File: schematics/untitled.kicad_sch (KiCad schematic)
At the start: 9 parts, among them U1 LM358, U2 LM358

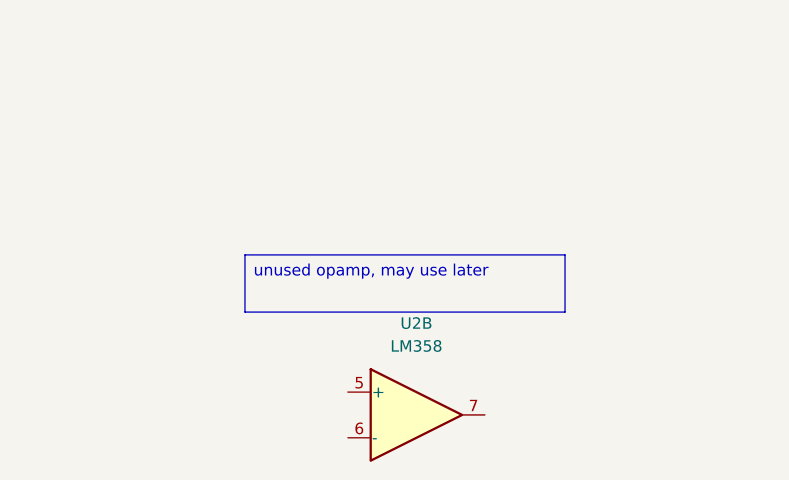
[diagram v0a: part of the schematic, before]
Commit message: added titles to all sheets
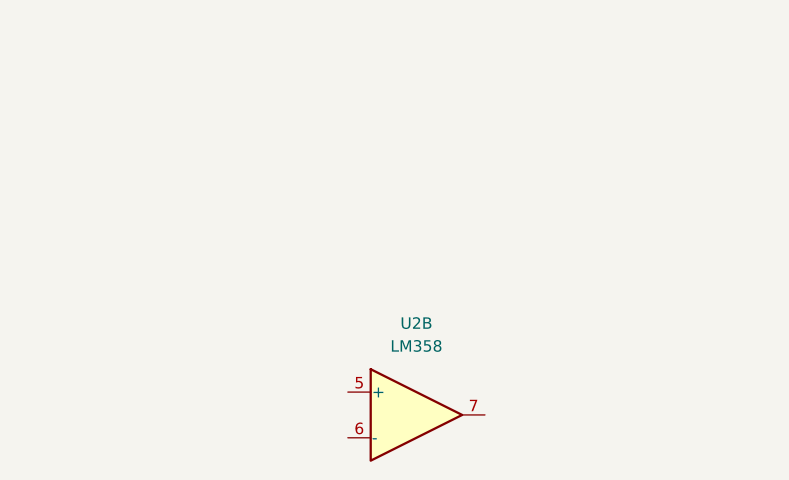
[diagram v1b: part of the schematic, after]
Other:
- company: (none) -> wish4snow
- title: (none) -> Thermocouple Decoder
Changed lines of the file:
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@@
 	(generator_version "9.0")
 	(paper "USLetter")
-	(text_box "unused opamp, may use later\n"
-		(exclude_from_sim no)
-		(at 106.68 177.8 0)
-		(size 35.56 6.35)
-		(margins 0.9525 0.9525 0.9525 0.9525)
-		(stroke
-			(width 0)
-			(type solid)
-		)
-		(fill
-			(type none)
-		)
-		(effects
-			(font
-				(size 1.27 1.27)
-			)
-			(justify left top)
-		)
+	(title_block
+		(title "Thermocouple Decoder")
+		(date "2026-01-22")
+		(rev "1")
+		(company "wish4snow")
+		(comment 1 "unused opamp, may use later")
 	)
 	(junction
